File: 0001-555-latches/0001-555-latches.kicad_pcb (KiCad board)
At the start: 2 copper layers, 88 x 75 mm, 37 parts, among them J1 DC_IN, J2 ASTBL_OUT, J3 BSTBL_OUT, J4 MSTBL_OUT, SW1 SW_Push, SW2 SW_Push, SW3 SW_Push, U1 NE555P, U2 NE555P, U3 NE555P

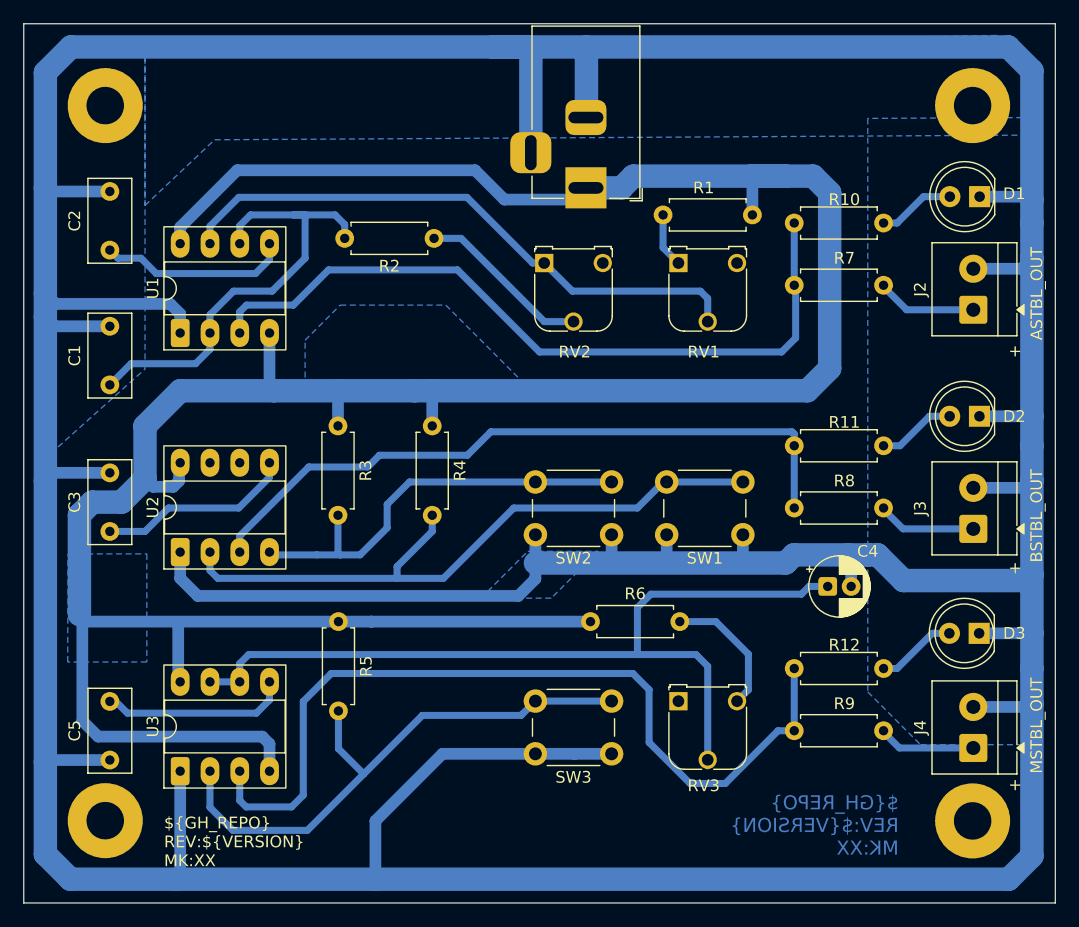
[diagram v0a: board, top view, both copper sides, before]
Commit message: Traces spacing corrections
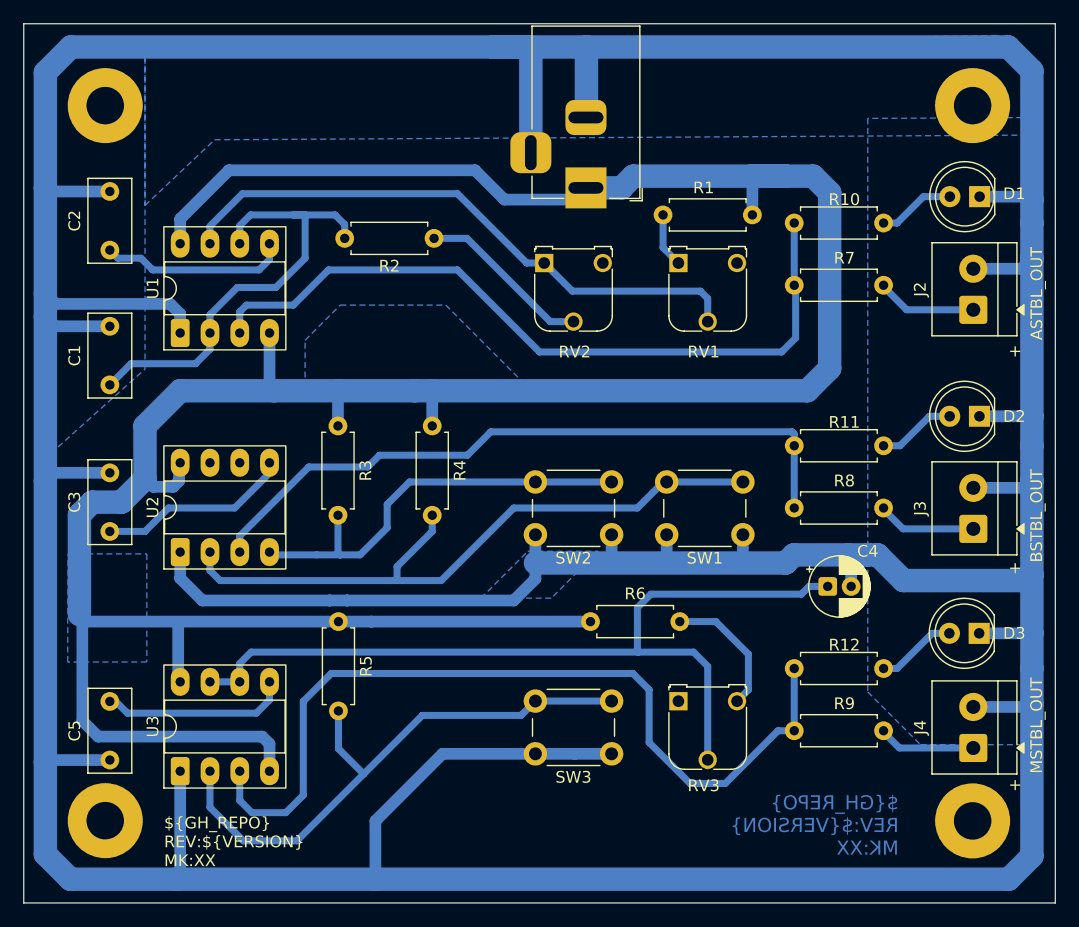
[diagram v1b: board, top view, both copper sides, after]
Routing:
- net Net-(U3-TR): track 49.0 -> 49.7 mm

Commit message: Update PCB
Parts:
- moved C4 1.08 mm to (168.5, 109.0)
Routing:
- net Net-(U3-DIS): track 74.2 -> 72.7 mm
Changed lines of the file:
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@@
 		(tenting front back)
 		(pcbplotparams
-			(layerselection 0x00000000_00000000_55555555_5755f5ff)
+			(layerselection 0x00000000_00000000_5555555d_5755557c)
 			(plot_on_all_layers_selection 0x00000000_00000000_00000000_00000000)
 			(disableapertmacros no)
@@
 			(outputformat 1)
 			(mirror no)
-			(drillshape 1)
+			(drillshape 0)
 			(scaleselection 1)
 			(outputdirectory "")
@@
 	(footprint "Capacitor_THT:CP_Radial_D5.0mm_P2.00mm"
 		(layer "F.Cu")
-		(at 169.580571 109)
+		(at 168.503058 109)
 		(descr "CP, Radial series, Radial, pin pitch=2.00mm, diameter=5mm, height=7mm, Electrolytic Capacitor")
 		(tags "CP Radial series Radial pin pitch 2.00mm diameter 5mm height 7mm Electrolytic Capacitor")
@@
 		)
 		(pad "1" thru_hole roundrect
-			(at 0 0)
+			(at -0.420071 -0.01)
 			(size 1.6 1.6)
 			(drill 0.8)
@@
 		)
 		(pad "2" thru_hole circle
-			(at 2 0)
+			(at 2.13 -0.01)
 			(size 1.6 1.6)
 			(drill 0.8)
@@
 			(font
 				(size 1.2 1.2)
-				(thickness 0.1875)
+				(thickness 0.24)
+				(bold yes)
 			)
 			(justify left bottom mirror)
@@
 	)
 	(gr_text "${GH_REPO}\nREV:${VERSION}\nMK:XX"
-		(at 112.965477 132.981216 0)
+		(at 114 134 0)
 		(layer "F.SilkS")
 		(effects
 			(font
-				(size 1 1)
-				(thickness 0.1)
+				(size 1.3 1.3)
+				(thickness 0.26)
+				(bold yes)
 			)
 			(justify left bottom)
@@
 	)
 	(segment
-		(start 171.580571 106.543522)
-		(end 171.345683 106.308634)
-		(width 1)
-		(layer "B.Cu")
-		(net 1)
-	)
-	(segment
 		(start 187 100)
 		(end 187 108)
@@
 	)
 	(segment
-		(start 166.691366 106.308634)
-		(end 171.345683 106.308634)
-		(width 2)
-		(layer "B.Cu")
-		(net 1)
-	)
-	(segment
 		(start 127.097318 110.2)
 		(end 116.237049 110.2)
@@
 	)
 	(segment
-		(start 173.845683 106.308634)
-		(end 176.037049 108.5)
+		(start 114 133.973046)
+		(end 104.973046 133.973046)
 		(width 2)
 		(layer "B.Cu")
@@
 	)
 	(segment
-		(start 114 133.973046)
-		(end 104.973046 133.973046)
-		(width 2)
+		(start 114.345683 124.758194)
+		(end 114.345683 133.627363)
+		(width 1)
 		(layer "B.Cu")
 		(net 1)
 	)
 	(segment
-		(start 166 107)
-		(end 144.646456 107)
+		(start 176.037049 108.5)
+		(end 173.845683 106.308634)
 		(width 2)
 		(layer "B.Cu")
@@
 	)
 	(segment
-		(start 114.345683 124.758194)
-		(end 114.345683 133.627363)
-		(width 1)
+		(start 164.691366 106.308634)
+		(end 164 107)
+		(width 2)
 		(layer "B.Cu")
 		(net 1)
@@
 	)
 	(segment
+		(start 187 108)
+		(end 186.5 108.5)
+		(width 2)
+		(layer "B.Cu")
+		(net 1)
+	)
+	(segment
 		(start 186.410444 100.589556)
 		(end 187 100)
@@
 	)
 	(segment
-		(start 176.037049 108.5)
-		(end 186.5 108.5)
-		(width 2)
-		(layer "B.Cu")
-		(net 1)
-	)
-	(segment
 		(start 185.026954 133.973046)
 		(end 131 133.973046)
@@
 	)
 	(segment
-		(start 173 106.308634)
-		(end 171.345683 106.308634)
-		(width 2)
-		(layer "B.Cu")
-		(net 1)
-	)
-	(segment
 		(start 114.345683 85.745683)
 		(end 113.5 84.9)
@@
 	)
 	(segment
+		(start 173.845683 106.308634)
+		(end 164.691366 106.308634)
+		(width 2)
+		(layer "B.Cu")
+		(net 1)
+	)
+	(segment
 		(start 144 62.981888)
 		(end 144.2575 63.239388)
@@
 	)
 	(segment
-		(start 171.580571 109)
-		(end 171.580571 106.543522)
+		(start 170.633058 108.99)
+		(end 170.633058 106.561692)
 		(width 1)
 		(layer "B.Cu")
@@
 	)
 	(segment
-		(start 144.2575 63.239388)
-		(end 144.2575 72)
+		(start 164 107)
+		(end 144.646456 107)
 		(width 2)
 		(layer "B.Cu")
@@
 	)
 	(segment
-		(start 173 106.308634)
-		(end 173.845683 106.308634)
+		(start 144.2575 63.239388)
+		(end 144.2575 72)
 		(width 2)
 		(layer "B.Cu")
@@
 	(segment
 		(start 186.5 108.5)
-		(end 187 108)
-		(width 2)
-		(layer "B.Cu")
-		(net 1)
-	)
-	(segment
-		(start 166.691366 106.308634)
-		(end 166 107)
+		(end 176.037049 108.5)
 		(width 2)
 		(layer "B.Cu")
@@
 	)
 	(segment
+		(start 170.633058 108.99)
+		(end 170.61 108.966942)
+		(width 1)
+		(layer "B.Cu")
+		(net 1)
+	)
+	(segment
 		(start 103.153317 75.308634)
 		(end 102.844683 75)
@@
 	)
 	(segment
-		(start 154.49529 109.659027)
-		(end 167.340973 109.659027)
+		(start 119.425683 115.574317)
+		(end 120.4 114.6)
 		(width 0.6)
 		(layer "B.Cu")
@@
 	)
 	(segment
-		(start 119.425683 115.574317)
-		(end 120.4 114.6)
+		(start 153.345683 114.545683)
+		(end 153.345683 110.808634)
 		(width 0.6)
 		(layer "B.Cu")
@@
 	)
 	(segment
-		(start 167.340973 109.659027)
-		(end 168 109)
+		(start 153.4 114.6)
+		(end 158.137049 114.6)
 		(width 0.6)
 		(layer "B.Cu")
@@
 	)
 	(segment
-		(start 153.345683 110.808634)
-		(end 153.345683 114.545683)
+		(start 168.072987 109)
+		(end 168.082987 108.99)
 		(width 0.6)
 		(layer "B.Cu")
@@
 	)
 	(segment
-		(start 153.345683 114.545683)
-		(end 153.4 114.6)
+		(start 154.49529 109.659027)
+		(end 165.340973 109.659027)
 		(width 0.6)
 		(layer "B.Cu")
@@
 	)
 	(segment
-		(start 153.4 114.6)
-		(end 158.137049 114.6)
+		(start 166 109)
+		(end 168.072987 109)
 		(width 0.6)
 		(layer "B.Cu")
@@
 	)
 	(segment
-		(start 168 109)
-		(end 169.580571 109)
+		(start 165.340973 109.659027)
+		(end 166 109)
+		(width 0.6)
+		(layer "B.Cu")
+		(net 5)
+	)
+	(segment
+		(start 153.345683 110.808634)
+		(end 154.49529 109.659027)
 		(width 0.6)
 		(layer "B.Cu")
@@
 	)
 	(segment
-		(start 158.137049 114.6)
-		(end 159.345683 115.808634)
+		(start 153.4 114.6)
+		(end 153.345683 114.545683)
 		(width 0.6)
 		(layer "B.Cu")
@@
 	)
 	(segment
-		(start 154.49529 109.659027)
-		(end 153.345683 110.808634)
+		(start 158.137049 114.6)
+		(end 159.345683 115.808634)
 		(width 0.6)
 		(layer "B.Cu")

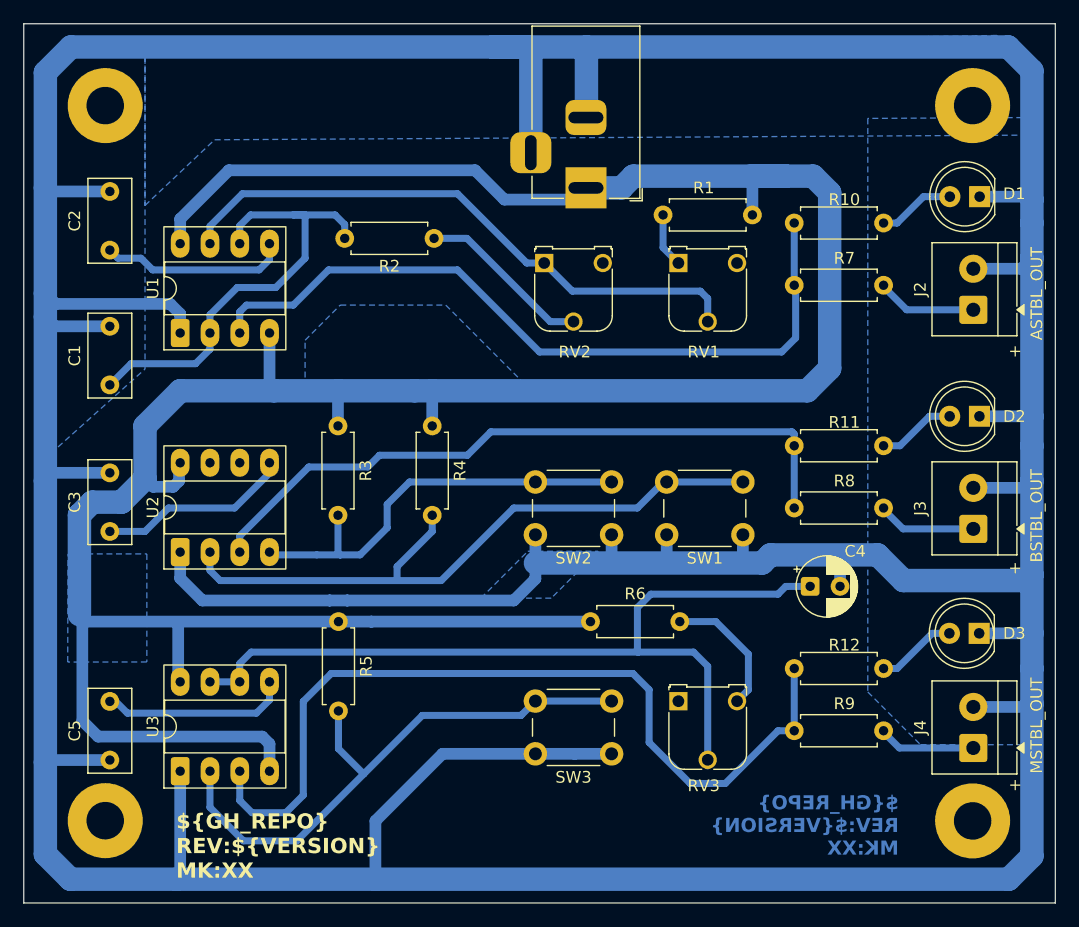
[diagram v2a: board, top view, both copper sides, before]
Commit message: Implementation (#5)
* Update GH organisation in PCB

* Correcting files

* Fix formatting

* Fix typo

---------

Co-authored-by: Marcin Ciapa <aaryndo@gmail.com>
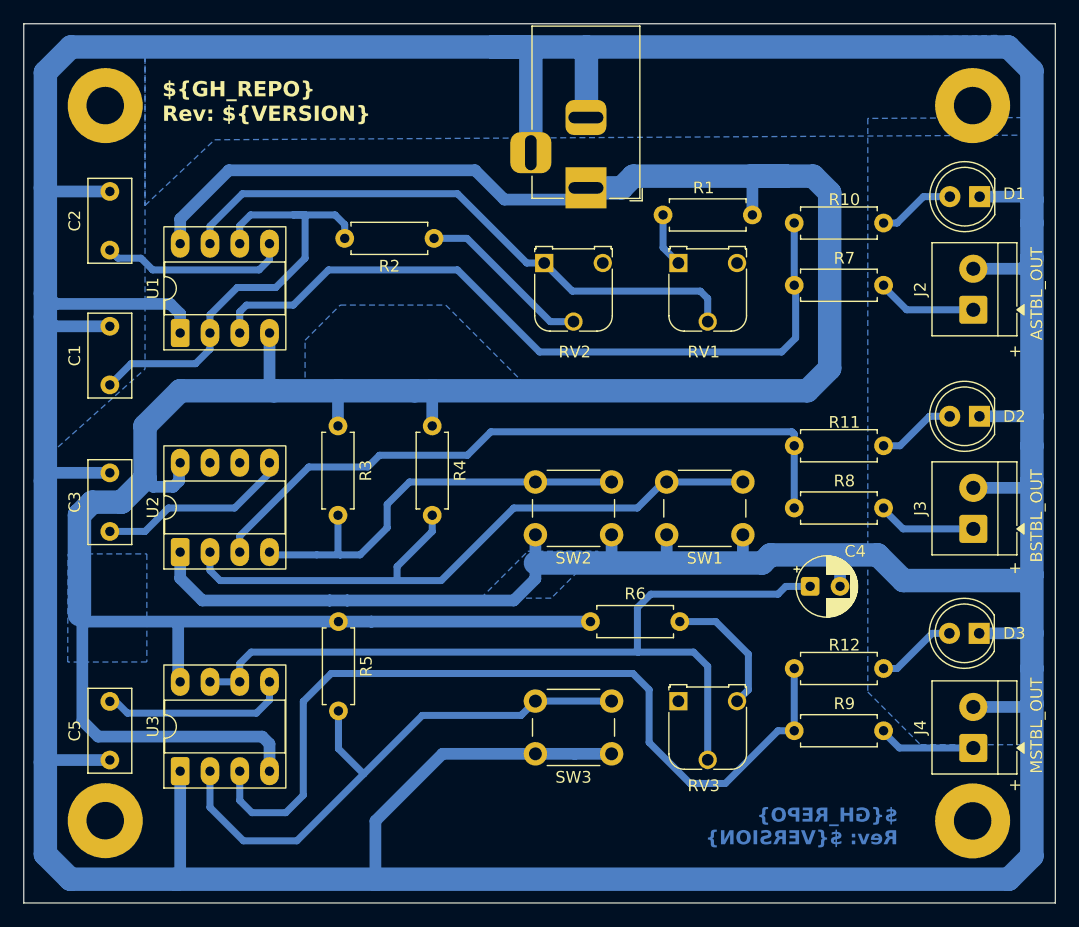
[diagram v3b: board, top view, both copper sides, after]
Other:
- board text added: "${GH_REPO} Rev: ${VERSION}"
- board text removed: "${GH_REPO} REV:${VERSION} MK:XX"
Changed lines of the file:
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@@
 		)
 	)
-	(property "GH_REPO" "https://github.com/marcinciapa-el/0001")
+	(property "GH_REPO" "github.com/mc-hw/0001")
 	(property "VERSION" "1.0.0")
 	(net 0 "")
@@
 		(layer "Edge.Cuts")
 	)
-	(gr_text "${GH_REPO}\nREV:${VERSION}\nMK:XX"
-		(at 175.644275 132.023504 0)
+	(gr_text "${GH_REPO}\nRev: ${VERSION}"
+		(at 175.57 131.14 0)
 		(layer "B.Cu")
 		(effects
@@
 		)
 	)
-	(gr_text "${GH_REPO}\nREV:${VERSION}\nMK:XX"
-		(at 114 134 0)
+	(gr_text "${GH_REPO}\nRev: ${VERSION}"
+		(at 112.813608 69.44284 0)
 		(layer "F.SilkS")
 		(effects

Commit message: Update labels on PCB
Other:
- board text added: "${GH_REPO} REV: ${VERSION}"
- board text removed: "${GH_REPO} Rev: ${VERSION}"
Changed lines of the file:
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@@
 		)
 	)
-	(property "GH_REPO" "github.com/mc-hw/0001")
-	(property "VERSION" "1.0.0")
+	(property "GH_REPO" "GITHUB.COM/MC-HW/0001")
+	(property "VERSION" "1.0.1")
 	(net 0 "")
 	(net 1 "GND")
@@
 		(layer "Edge.Cuts")
 	)
-	(gr_text "${GH_REPO}\nRev: ${VERSION}"
-		(at 175.57 131.14 0)
+	(gr_text "${GH_REPO}\nREV: ${VERSION}"
+		(at 177.1 131.88 0)
 		(layer "B.Cu")
 		(effects
 			(font
-				(size 1.2 1.2)
-				(thickness 0.24)
+				(size 1.5 1.5)
+				(thickness 0.3)
+				(bold yes)
+			)
+			(justify left bottom mirror)
+		)
+	)
+	(gr_text "${GH_REPO}\nREV: ${VERSION}"
+		(at 142.77 69.39 0)
+		(layer "B.Mask")
+		(effects
+			(font
+				(size 1.5 1.5)
+				(thickness 0.3)
 				(bold yes)
 			)
@@
 		)
 	)
-	(gr_text "${GH_REPO}\nRev: ${VERSION}"
-		(at 112.813608 69.44284 0)
+	(gr_text "${GH_REPO}\nREV: ${VERSION}"
+		(at 112.28 69.6 0)
 		(layer "F.SilkS")
 		(effects
 			(font
-				(size 1.3 1.3)
-				(thickness 0.26)
+				(size 1.5 1.5)
+				(thickness 0.3)
 				(bold yes)
 			)
